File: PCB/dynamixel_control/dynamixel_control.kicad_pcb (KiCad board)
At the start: 4 copper layers, 36 x 56 mm, 59 parts, among them J1 12V, J11 Dynamixel TTL, J12 Dynamixel TTL, J2 RS232, J6 Debug Uart, J8 Dynamixel TTL, Q1 SSM3J372R, Q2 IPD068P03L3GATMA1, Q3 T2N7002AK, SW1 LIMIT_SWITCH, U1 R-78E5.0-0.5, U2 SN74AHC1G14, U3 LM810M3-4.63, U4 Teensy_4.0, U5 SN65C3221E, U6 ICM-40627, U7 SN74LV1T34, U8 SN74LVC2G241

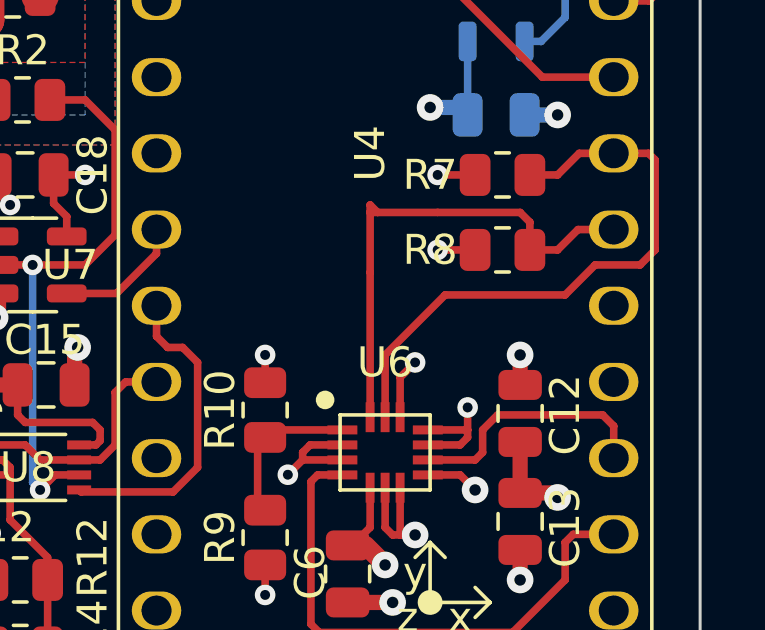
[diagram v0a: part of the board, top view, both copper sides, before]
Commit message: Fix dynamixel_control weird traces
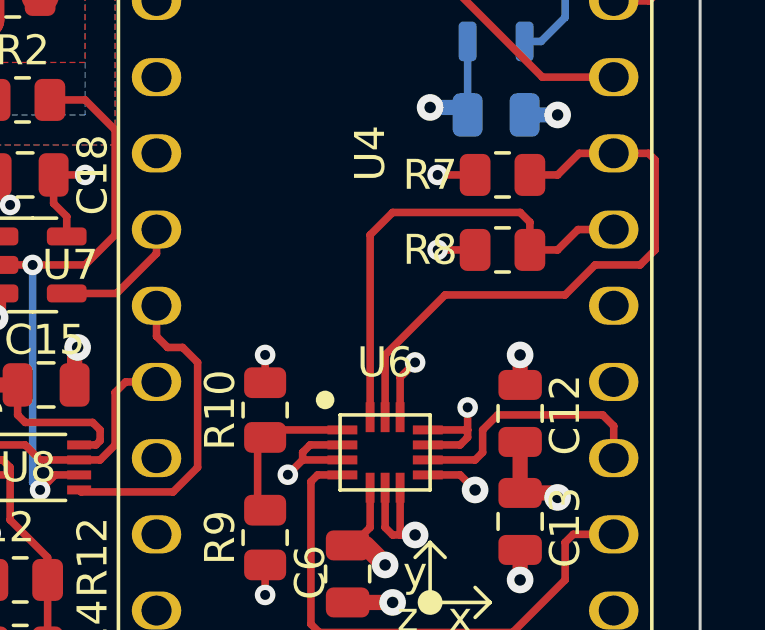
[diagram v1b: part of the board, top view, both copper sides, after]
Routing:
- net /I2C_SDA: track 17.2 -> 16.1 mm
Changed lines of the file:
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@@
   (segment (start 50.325 59) (end 51.25 59) (width 0.254) (layer "F.Cu") (net 18))
   (segment (start 51.5 63) (end 47.5 63) (width 0.254) (layer "F.Cu") (net 18))
-  (segment (start 45.25 60.25) (end 45 60.25) (width 0.254) (layer "F.Cu") (net 19))
-  (segment (start 50 60.25) (end 50.325 60.575) (width 0.254) (layer "F.Cu") (net 19))
+  (segment (start 45.75 60.25) (end 45 61) (width 0.254) (layer "F.Cu") (net 19))
   (segment (start 51.93 60.82) (end 51.25 61.5) (width 0.254) (layer "F.Cu") (net 19))
   (segment (start 51.25 61.5) (end 50.325 61.5) (width 0.254) (layer "F.Cu") (net 19))
-  (segment (start 47.25 60.25) (end 50 60.25) (width 0.254) (layer "F.Cu") (net 19))
-  (segment (start 45 60) (end 45.25 60.25) (width 0.254) (layer "F.Cu") (net 19))
+  (segment (start 50.325 60.575) (end 50 60.25) (width 0.254) (layer "F.Cu") (net 19))
   (segment (start 53.12 60.82) (end 51.93 60.82) (width 0.254) (layer "F.Cu") (net 19))
-  (segment (start 45 67.3375) (end 45 62.25) (width 0.254) (layer "F.Cu") (net 19))
-  (segment (start 45 62.25) (end 45 60.25) (width 0.254) (layer "F.Cu") (net 19))
-  (segment (start 50.325 60.575) (end 50.325 61.5) (width 0.254) (layer "F.Cu") (net 19))
-  (segment (start 45 60.25) (end 45 60) (width 0.254) (layer "F.Cu") (net 19))
-  (segment (start 45.25 60.25) (end 47.25 60.25) (width 0.254) (layer "F.Cu") (net 19))
+  (segment (start 50 60.25) (end 45.75 60.25) (width 0.254) (layer "F.Cu") (net 19))
+  (segment (start 45 61) (end 45 67.3375) (width 0.254) (layer "F.Cu") (net 19))
+  (segment (start 50.325 61.5) (end 50.325 60.575) (width 0.254) (layer "F.Cu") (net 19))
   (segment (start 23.25 73) (end 23.25 74.623) (width 0.254) (layer "F.Cu") (net 20))
   (segment (start 23.25 73) (end 23.25 67.25) (width 0.254) (layer "F.Cu") (net 20))

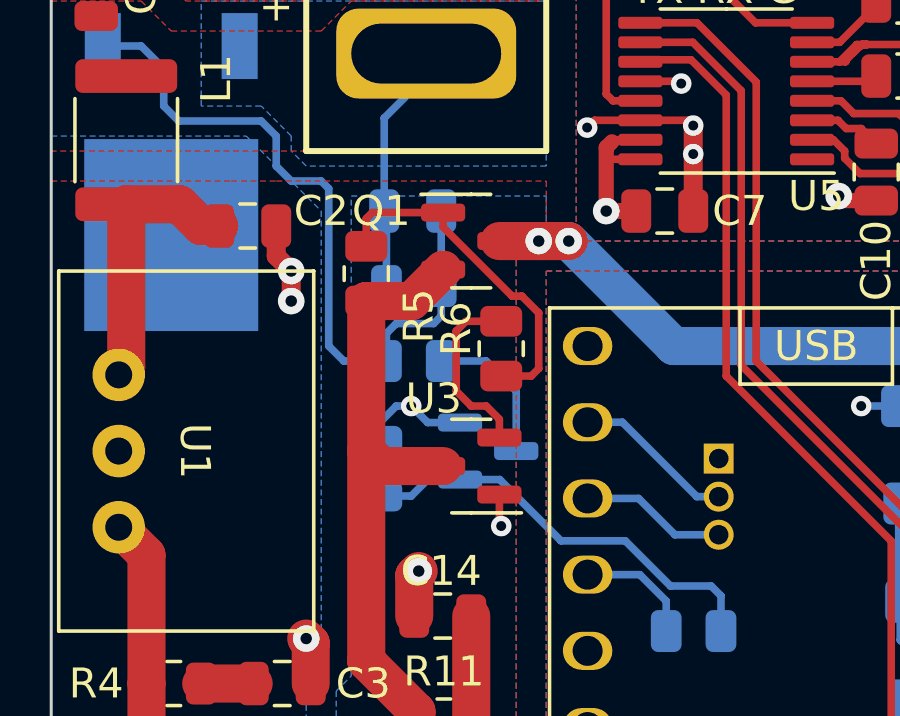
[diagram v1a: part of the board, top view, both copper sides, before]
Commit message: Remove voltage supervisors
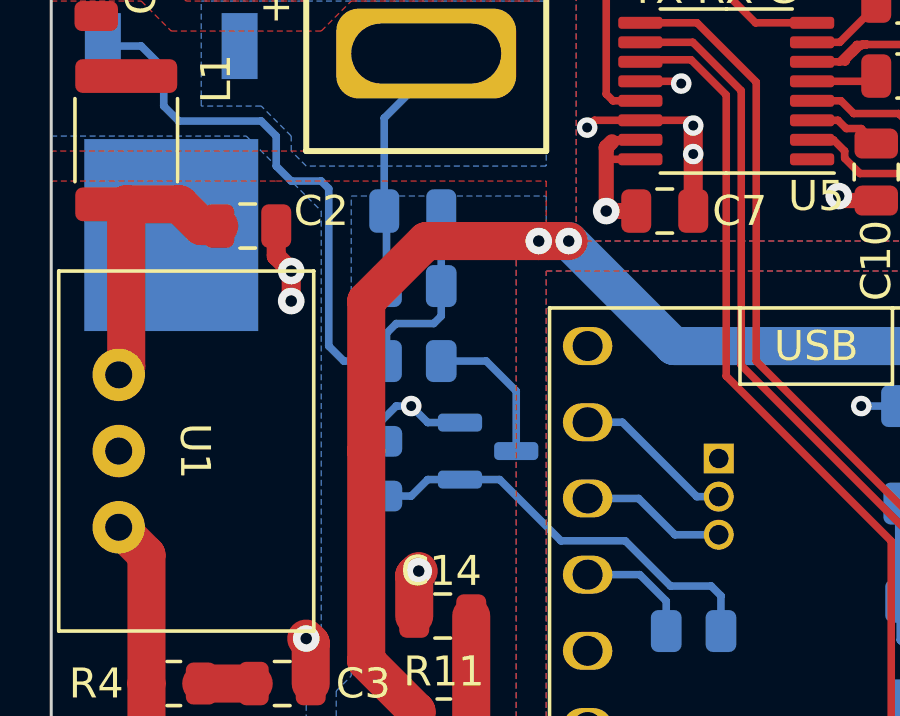
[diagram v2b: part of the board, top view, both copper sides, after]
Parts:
- removed Q1: SSM3J372R, Package_TO_SOT_SMD:SOT-23
- removed R5: 100k, Resistor_SMD:R_0805_2012Metric
- removed R6: 511, Resistor_SMD:R_0805_2012Metric
- removed U3: LM810M3-4.63, Package_TO_SOT_SMD:SOT-23
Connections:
- U4 pad VIN: Net-(Q1-Pad3) -> +5V
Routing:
- net Net-(Q1-Pad3): track 19.6 -> 0.00 mm, vias 2 -> 0
- net +5V: track 52.5 -> 71.6 mm, vias 0 -> 2
- net Net-(Q1-Pad1): track 11.6 -> 0.00 mm
- net Net-(R6-Pad1): track 6.07 -> 0.00 mm
- net GND: track 53.1 -> 52.0 mm, vias 38 -> 37
